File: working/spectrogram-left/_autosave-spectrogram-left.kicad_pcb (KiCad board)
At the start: 2 copper layers, 135.7 x 99.4 mm, 107 parts, among them U2 ProMicro

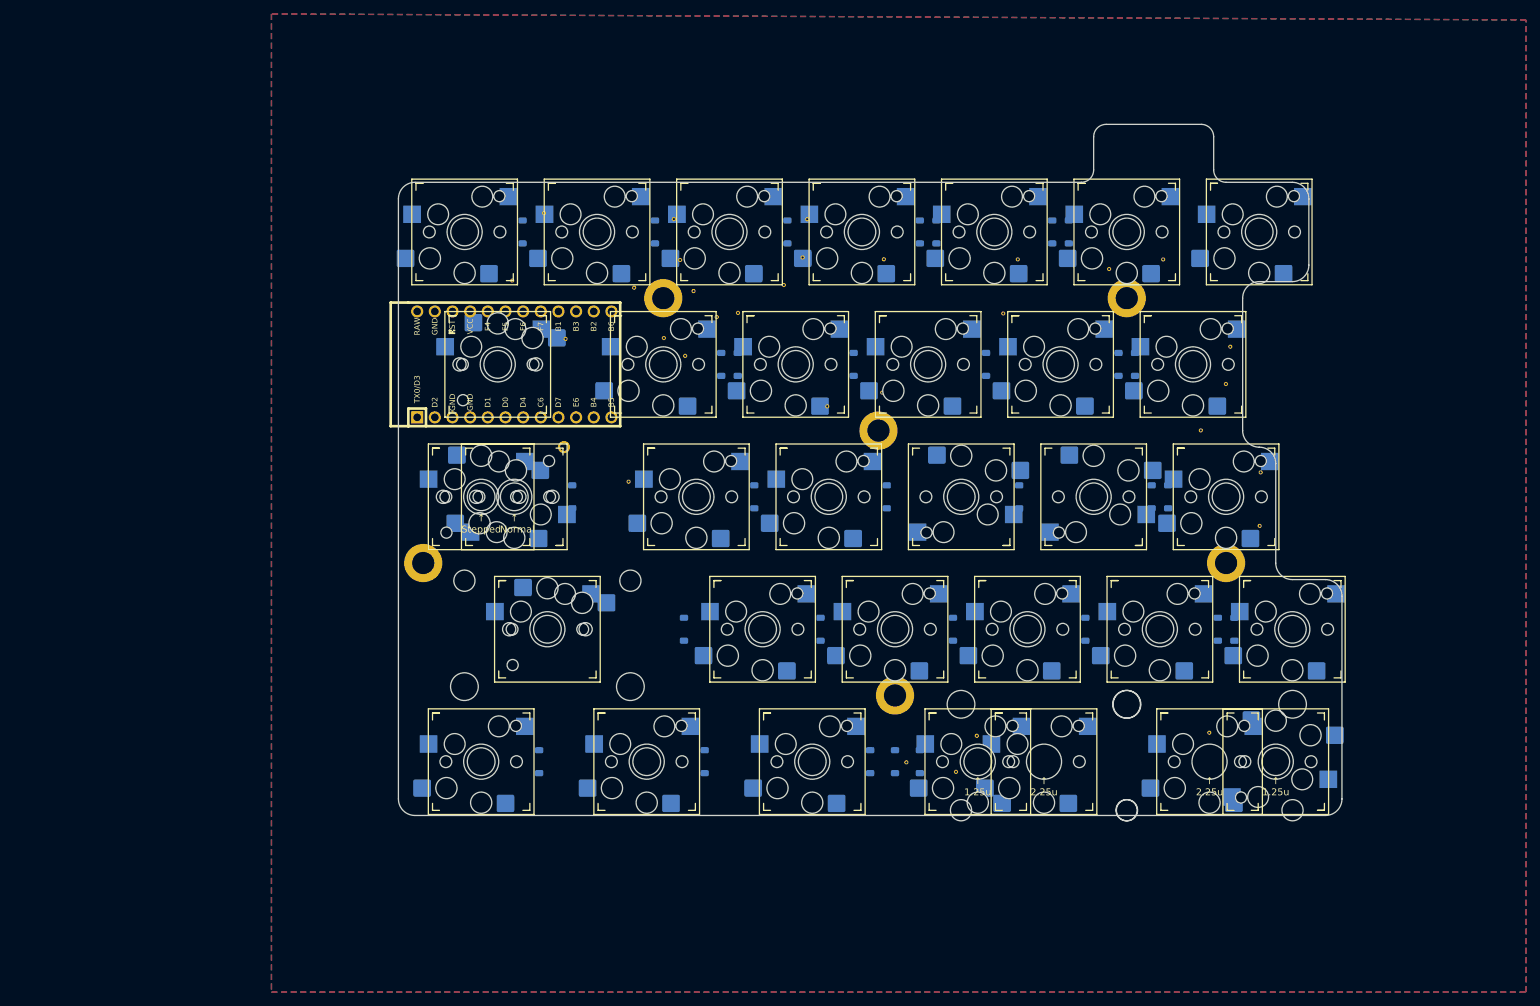
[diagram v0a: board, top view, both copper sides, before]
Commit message: changed footprints, still have to route
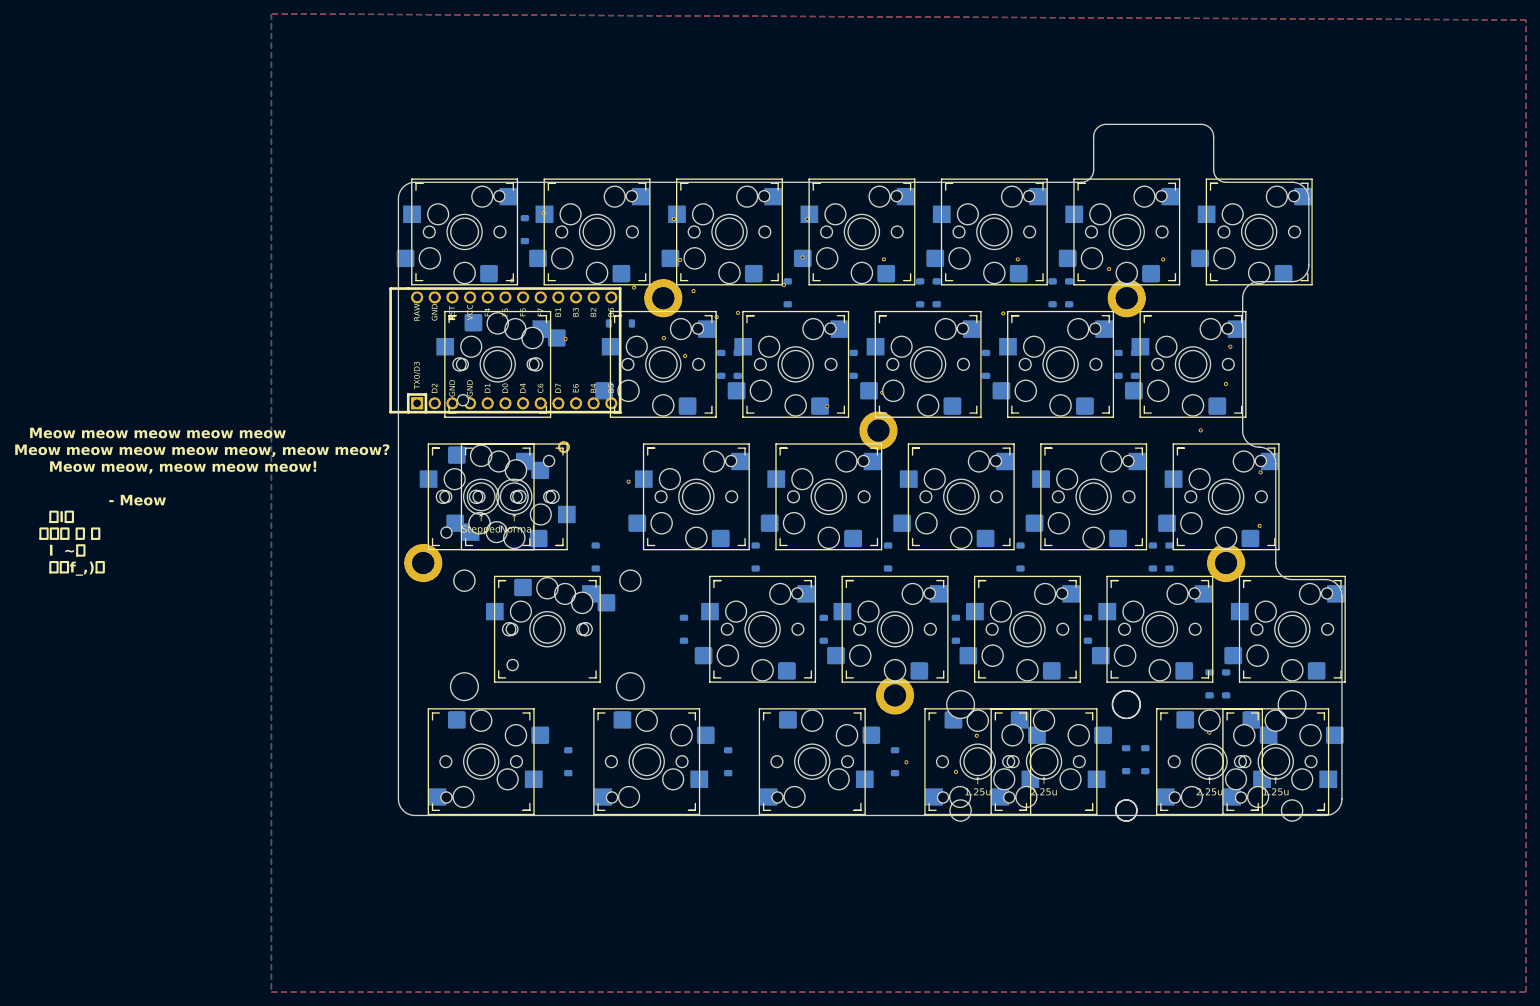
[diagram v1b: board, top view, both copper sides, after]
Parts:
- SW_E1, SW_E2, SW_E3, SW_E7: footprint jakestuff:ChocMX_flippedpads -> jakestuff:ChocMX
- SW_E5, SW_EB7: footprint jakestuff:ChocMX_flippedpads_2.25U -> jakestuff:ChocMX_flippedpads_2.25U_reversedstab
- moved D_E7 36.0 mm to (131.2, 109.2)
- moved D_E5 29.7 mm to (128.5, 109.2)
- moved D_A2 14.1 mm to (55.8, 46.5), turned to 0 degrees
- moved D_C1 9.30 mm to (52.2, 80.1)
- moved D_A3 8.76 mm to (79.8, 42.1)
- moved D_A4 8.76 mm to (98.9, 42.1)
- moved D_A5 8.76 mm to (101.2, 42.1)
- moved D_A6 8.76 mm to (120.3, 42.1)
- moved D_A7 8.76 mm to (117.9, 42.1)
- moved D_C2 8.66 mm to (75.2, 80.1)
- moved D_C3 8.66 mm to (94.2, 80.1)
- moved D_C4 8.66 mm to (113.3, 80.1)
- moved D_C5 8.66 mm to (132.3, 80.1)
- moved D_C6 8.66 mm to (134.7, 80.1)
- moved D_D6 7.95 mm to (140.5, 98.3)
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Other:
- board text added: "Meow meow meow meow meow Meow meow meow meow meow, meow meow? Meow meow, meow meow meow! - Meow ／l、 （ﾟ､ ｡ ７ l ~ヽ じしf_,)ノ"
